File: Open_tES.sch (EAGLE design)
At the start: 59 parts, among them IC2 MAX232ECWES, IC4 LP2950CZ-5.0, IC5 OPA277U, IC6 LF444CM, IC7 PIC16F1937P, J1 RJ11-2X, U1 MIC2288YD5-TR, U2 74LVC1G10W6-7, X1 22-23-2041, X2 057-016-1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

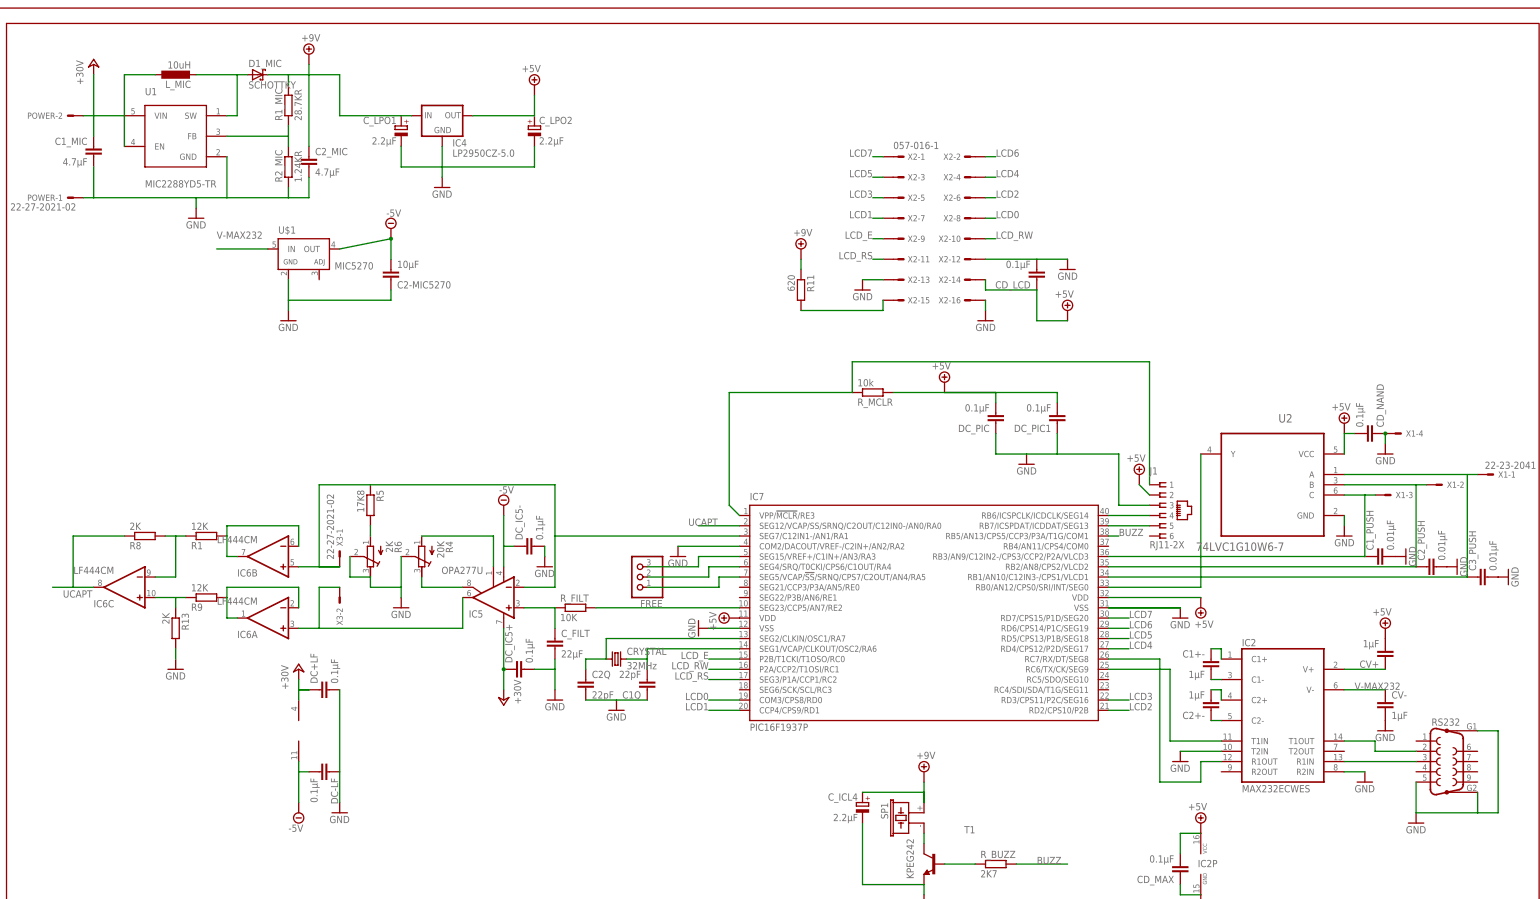
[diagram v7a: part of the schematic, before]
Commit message: fixing of connecting error +9V and +30V. MIC2288 and LP2950 was concerned. Correction of capacitor for LPO.
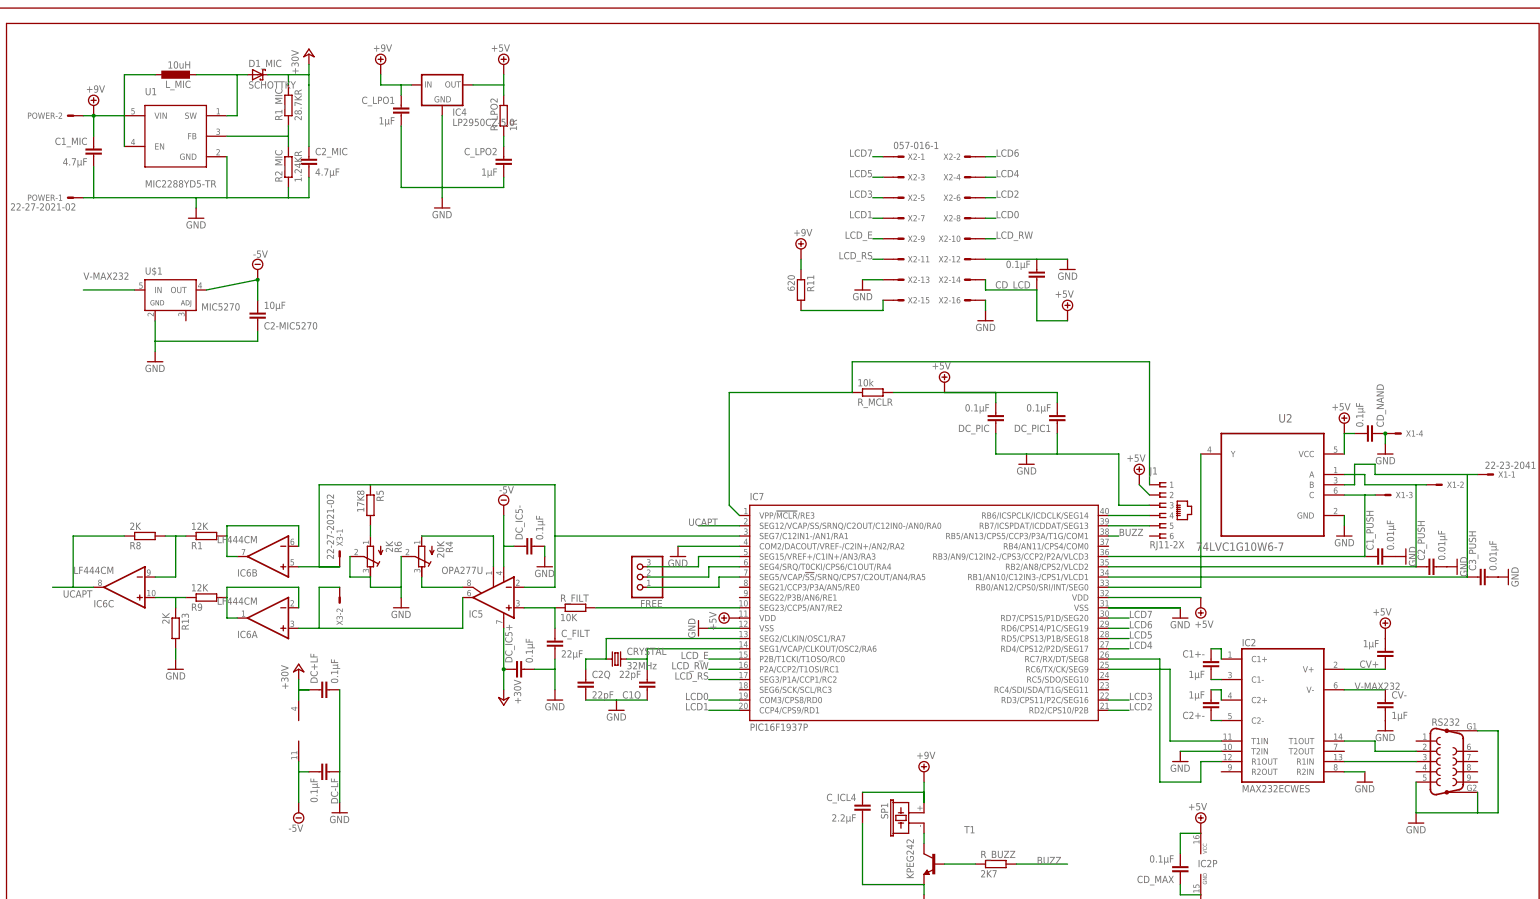
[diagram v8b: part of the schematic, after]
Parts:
- added R_LPO2: 1R, rcl:R-EU_R0805
- C_ICL4: device rcl:CPOL-EUE1.8-4 -> rcl:C-EUC0805K; OC_FARNELL 8766983 -> 9227822
- C_LPO1, C_LPO2: value 2.2µF -> 1µF; device rcl:CPOL-EUE1.8-4 -> rcl:C-EUC0805; OC_FARNELL 8766983 -> 2496946
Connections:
- new net N$21: C_LPO2.1, R_LPO2.1
- net +24V: now also C2_MIC.1, D1_MIC.C, R1_MIC.2; no longer C1_MIC.1, L_MIC.1, POWER-2.S, U1.EN, U1.VIN
- net +5V/1: now also R_LPO2.2; no longer C_LPO2.+
- net +9V: now also C1_MIC.1, C_ICL4.1, C_LPO1.1, L_MIC.1, POWER-2.S, U1.EN, U1.VIN; no longer C2_MIC.1, C_ICL4.+, C_LPO1.+, D1_MIC.C, R1_MIC.2
- net GND: now also C_ICL4.2, C_LPO1.2, C_LPO2.2; no longer C_ICL4.-, C_LPO1.-, C_LPO2.-
- net N$23: now also U2.A; no longer U2.B
- net N$9: now also U2.B; no longer U2.A
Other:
- moved on the sheet: C2-MIC5270, IC4, U$1
